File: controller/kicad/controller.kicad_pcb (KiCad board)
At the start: 2 copper layers, 132.3 x 80.9 mm, 6 parts, among them J1 pcie_98, J2 pcie_98, J3 pcie_98, J4 pcie_98, J5 pcie_98

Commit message: Auto update of the files of controller/kicad to complete the rename from main_board.
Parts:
- J1, J2, J3, J4, J5: footprint main_board:pcie_98_socket -> controller:pcie_98_socket
- RN1: footprint main_board:weact_stm32fh750 -> controller:weact_stm32fh750
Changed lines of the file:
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@@
   (net 11 "unconnected-(RN1-R2.2-Pad11)")
   (net 12 "unconnected-(RN1-R1.2-Pad12)")
-  (footprint "main_board:pcie_98_socket" (layer "F.Cu")
+  (footprint "controller:pcie_98_socket" (layer "F.Cu")
     (at 93.9 37.000004 -90)
     (tags "9-1734774-5 ")
-    (property "Sheetfile" "main_board.kicad_sch")
+    (property "Sheetfile" "controller.kicad_sch")
     (property "Sheetname" "")
     (property "ki_description" "Generic connector, double row, 02x32, row letter first pin numbering scheme (pin number consists of a letter for the row and a number for the pin index in this row. a1, ..., aN; b1, ..., bN), script generated (kicad-library-utils/schlib/autogen/connector/)")
@@
     )
   )
-  (footprint "main_board:pcie_98_socket" (layer "F.Cu")
+  (footprint "controller:pcie_98_socket" (layer "F.Cu")
     (at 109.4 36.800004 -90)
     (tags "9-1734774-5 ")
-    (property "Sheetfile" "main_board.kicad_sch")
+    (property "Sheetfile" "controller.kicad_sch")
     (property "Sheetname" "")
     (property "ki_description" "Generic connector, double row, 02x32, row letter first pin numbering scheme (pin number consists of a letter for the row and a number for the pin index in this row. a1, ..., aN; b1, ..., bN), script generated (kicad-library-utils/schlib/autogen/connector/)")
@@
     )
   )
-  (footprint "main_board:pcie_98_socket" (layer "F.Cu")
+  (footprint "controller:pcie_98_socket" (layer "F.Cu")
     (at 138.35 36.900004 -90)
     (tags "9-1734774-5 ")
-    (property "Sheetfile" "main_board.kicad_sch")
+    (property "Sheetfile" "controller.kicad_sch")
     (property "Sheetname" "")
     (property "ki_description" "Generic connector, double row, 02x32, row letter first pin numbering scheme (pin number consists of a letter for the row and a number for the pin index in this row. a1, ..., aN; b1, ..., bN), script generated (kicad-library-utils/schlib/autogen/connector/)")
@@
     )
   )
-  (footprint "main_board:pcie_98_socket" (layer "F.Cu")
+  (footprint "controller:pcie_98_socket" (layer "F.Cu")
     (at 79.4 37.100004 -90)
     (tags "9-1734774-5 ")
-    (property "Sheetfile" "main_board.kicad_sch")
+    (property "Sheetfile" "controller.kicad_sch")
     (property "Sheetname" "")
     (property "ki_description" "Generic connector, double row, 02x32, row letter first pin numbering scheme (pin number consists of a letter for the row and a number for the pin index in this row. a1, ..., aN; b1, ..., bN), script generated (kicad-library-utils/schlib/autogen/connector/)")
@@
     )
   )
-  (footprint "main_board:weact_stm32fh750" (layer "F.Cu")
+  (footprint "controller:weact_stm32fh750" (layer "F.Cu")
     (at 39.6 62.05)
     (descr "Through hole straight pin header, 2x22, 2.54mm pitch, double rows")
     (tags "Through hole pin header THT 2x22 2.54mm double row")
-    (property "Sheetfile" "main_board.kicad_sch")
+    (property "Sheetfile" "controller.kicad_sch")
     (property "Sheetname" "")
     (property "ki_description" "6 resistor network, parallel topology")
@@
     )
   )
-  (footprint "main_board:pcie_98_socket" (layer "F.Cu")
+  (footprint "controller:pcie_98_socket" (layer "F.Cu")
     (at 123.9 36.85 -90)
     (tags "9-1734774-5 ")
-    (property "Sheetfile" "main_board.kicad_sch")
+    (property "Sheetfile" "controller.kicad_sch")
     (property "Sheetname" "")
     (property "ki_description" "Generic connector, double row, 02x32, row letter first pin numbering scheme (pin number consists of a letter for the row and a number for the pin index in this row. a1, ..., aN; b1, ..., bN), script generated (kicad-library-utils/schlib/autogen/connector/)")

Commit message: Work in progress. Controller schematic.
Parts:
- removed J1, J3, J4, J5: pcie_98, controller:pcie_98_socket
- removed RN1: R_Pack06, controller:weact_stm32fh750
- added D1: ESD, Diode_SMD:D_0402_1005Metric, F.Cu at (62.2, 42.9)
- added D2: ESD, Diode_SMD:D_0402_1005Metric, F.Cu at (62.2, 40.3)
- added D3: ESD, Diode_SMD:D_0402_1005Metric, F.Cu at (63.8, 43.0)
- added D4: ESD, Diode_SMD:D_0402_1005Metric, F.Cu at (63.8, 40.4)
- added D5: ESD, Diode_SMD:D_0402_1005Metric, F.Cu at (51.2, 43.3)
- added D6: ESD, Diode_SMD:D_0402_1005Metric, F.Cu at (51.2, 45.3)
- added D7: ESD, Diode_SMD:D_0402_1005Metric, F.Cu at (51.2, 47.3)
- added D8: ESD, Diode_SMD:D_0402_1005Metric, F.Cu at (51.2, 49.2)
- added D9: ESD, Diode_SMD:D_0402_1005Metric, F.Cu at (51.2, 51.2)
- added U1: WeAct_STM32H750_Module, controller:weact_stm32fh750, F.Cu at (85.2, -5.38)
- J2: footprint controller:pcie_98_socket -> controller:pcie_98_edge
- moved J2 26.3 mm to (72.5, 62.5), turned to 0 degrees
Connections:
- J2 pad A1: (no net) -> GND
- J2 pad A10: (no net) -> /A
- J2 pad A11: (no net) -> /A
- J2 pad A12: (no net) -> /A
- J2 pad A13: (no net) -> /A
- J2 pad A14: (no net) -> /A
- J2 pad A15: (no net) -> /A
- J2 pad A16: (no net) -> /A
- J2 pad A17: (no net) -> /A
- J2 pad A18: (no net) -> /A
- J2 pad A19: (no net) -> /A
- J2 pad A2: (no net) -> GND
- J2 pad A20: (no net) -> /A
- J2 pad A21: (no net) -> /A
- J2 pad A22: (no net) -> /A
- J2 pad A23: (no net) -> /A
- J2 pad A24: (no net) -> /A
- J2 pad A25: (no net) -> /A
- J2 pad A26: (no net) -> /A
- J2 pad A27: (no net) -> /A
- J2 pad A28: (no net) -> /A
- J2 pad A29: (no net) -> /A
- J2 pad A3: (no net) -> GND
- J2 pad A30: (no net) -> /A
- J2 pad A31: (no net) -> /A
- J2 pad A32: (no net) -> /A
- J2 pad A33: (no net) -> /A
- J2 pad A34: (no net) -> /A
- J2 pad A35: (no net) -> /A
- J2 pad A36: (no net) -> /A
- J2 pad A37: (no net) -> /A
- J2 pad A38: (no net) -> /A
- J2 pad A39: (no net) -> /A
- J2 pad A4: (no net) -> GND
- J2 pad A40: (no net) -> /A
- J2 pad A41: (no net) -> /A
- J2 pad A42: (no net) -> /A
- J2 pad A43: (no net) -> /A
- J2 pad A44: (no net) -> /A
- J2 pad A45: (no net) -> /A
- J2 pad A46: (no net) -> /A
- J2 pad A47: (no net) -> /A
- J2 pad A48: (no net) -> /VIN-
- J2 pad A49: (no net) -> /VIN-
- J2 pad A5: (no net) -> /PE0
- J2 pad A6: (no net) -> /PB8
- J2 pad A7: (no net) -> /PB6
- J2 pad A8: (no net) -> /PB4
- J2 pad A9: (no net) -> /PD7
- J2 pad B1: (no net) -> +5V
- J2 pad B10: (no net) -> /B
- J2 pad B11: (no net) -> /B
- J2 pad B12: (no net) -> /B
- J2 pad B13: (no net) -> /B
- J2 pad B14: (no net) -> /B
- J2 pad B15: (no net) -> /B
- J2 pad B16: (no net) -> /B
- J2 pad B17: (no net) -> /B
- J2 pad B18: (no net) -> /B
- J2 pad B19: (no net) -> /B
- J2 pad B2: (no net) -> +5V
- J2 pad B20: (no net) -> /B
- J2 pad B21: (no net) -> /B
- J2 pad B22: (no net) -> /B
- J2 pad B23: (no net) -> /B
- J2 pad B3: (no net) -> +5V
- J2 pad B4: (no net) -> +5V
- J2 pad B5: (no net) -> /PE1
- J2 pad B6: (no net) -> /PB9
- J2 pad B7: (no net) -> /PB7
- J2 pad B8: (no net) -> /PB5
- J2 pad B9: (no net) -> /PB3
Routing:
- net /PE1: track 0.00 -> 97.2 mm
- net /PB9: track 0.00 -> 95.1 mm
- net /PB5: track 0.00 -> 20.9 mm
- net /PB7: track 0.00 -> 17.8 mm
- net GND: track 0.00 -> 1.77 mm, vias 0 -> 4
- net (no net): vias 0 -> 1
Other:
- board size 132.3 x 80.9 mm -> 58.6 x 9.3 mm

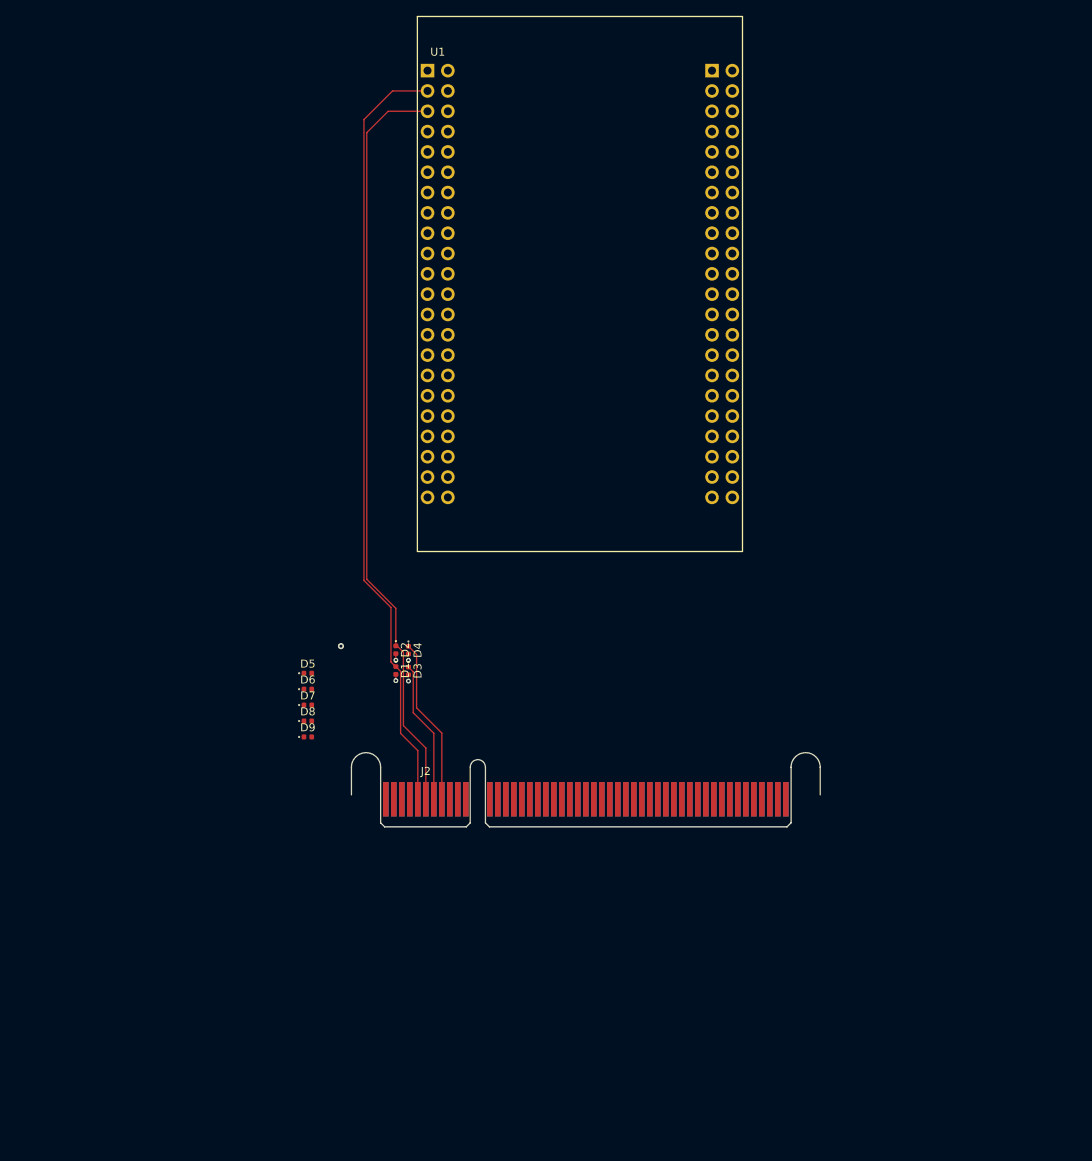
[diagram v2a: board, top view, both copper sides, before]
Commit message: Controller design in progress. Added ESD diode arrays.
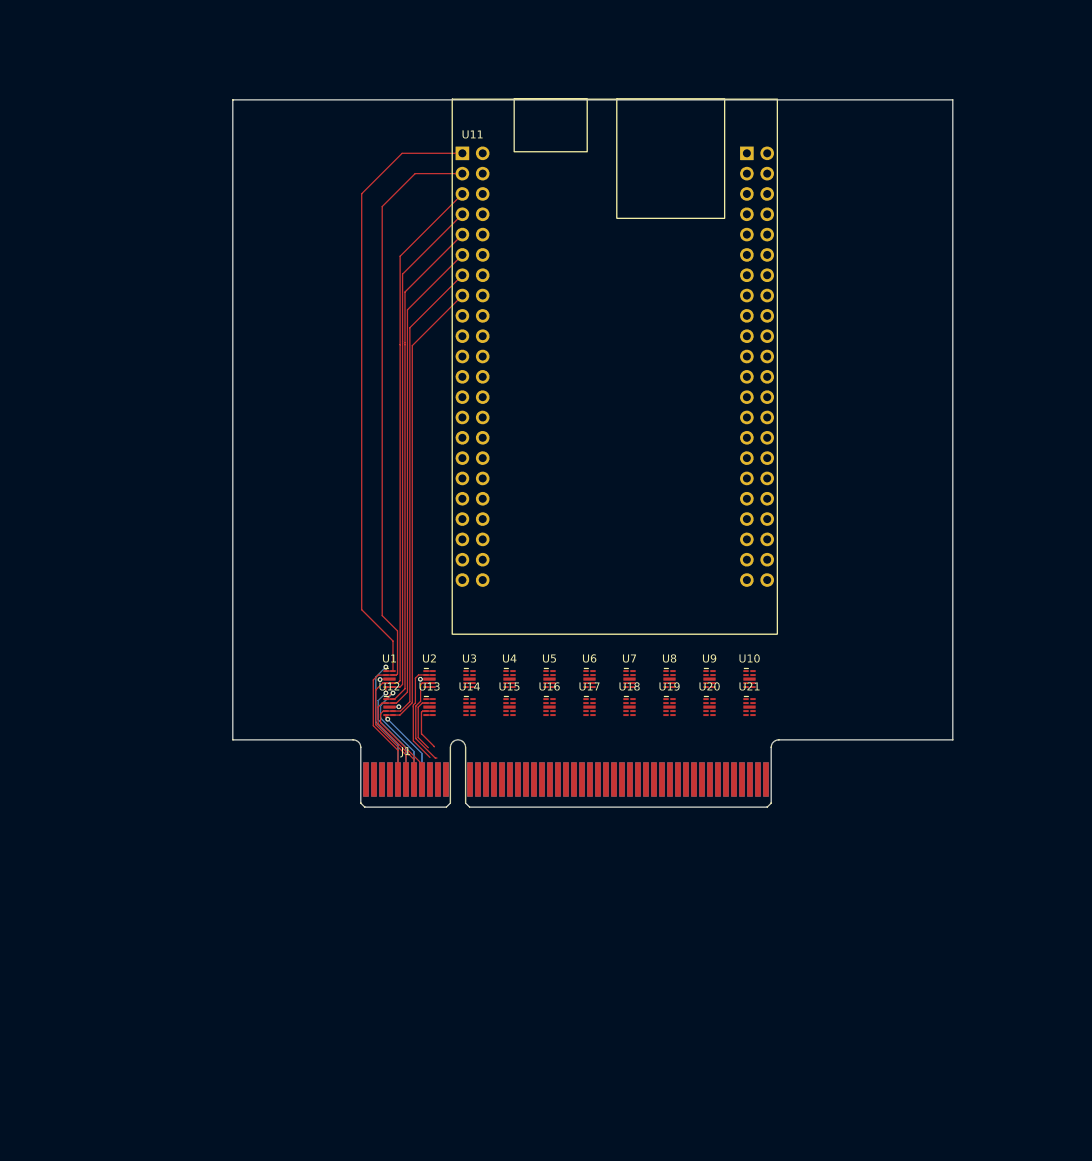
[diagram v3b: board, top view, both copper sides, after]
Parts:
- removed D1, D2, D3, D4, D5, D6, D7, D8, D9: ESD, Diode_SMD:D_0402_1005Metric
- added U1: ESD5344D, controller:Diodes_UDFN-10_1.0x2.5mm_P0.5mm, F.Cu at (61.4, 44.0)
- added U10: ESD5344D, controller:Diodes_UDFN-10_1.0x2.5mm_P0.5mm, F.Cu at (106.4, 44.0)
- added U12: ESD5344D, controller:Diodes_UDFN-10_1.0x2.5mm_P0.5mm, F.Cu at (61.4, 47.5)
- added U13: ESD5344D, controller:Diodes_UDFN-10_1.0x2.5mm_P0.5mm, F.Cu at (66.4, 47.5)
- added U14: ESD5344D, controller:Diodes_UDFN-10_1.0x2.5mm_P0.5mm, F.Cu at (71.4, 47.5)
- added U15: ESD5344D, controller:Diodes_UDFN-10_1.0x2.5mm_P0.5mm, F.Cu at (76.4, 47.5)
- added U16: ESD5344D, controller:Diodes_UDFN-10_1.0x2.5mm_P0.5mm, F.Cu at (81.4, 47.5)
- added U17: ESD5344D, controller:Diodes_UDFN-10_1.0x2.5mm_P0.5mm, F.Cu at (86.4, 47.5)
- added U18: ESD5344D, controller:Diodes_UDFN-10_1.0x2.5mm_P0.5mm, F.Cu at (91.4, 47.5)
- added U19: ESD5344D, controller:Diodes_UDFN-10_1.0x2.5mm_P0.5mm, F.Cu at (96.4, 47.5)
- added U2: ESD5344D, controller:Diodes_UDFN-10_1.0x2.5mm_P0.5mm, F.Cu at (66.4, 44.0)
- added U20: ESD5344D, controller:Diodes_UDFN-10_1.0x2.5mm_P0.5mm, F.Cu at (101.4, 47.5)
- added U21: ESD5344D, controller:Diodes_UDFN-10_1.0x2.5mm_P0.5mm, F.Cu at (106.4, 47.5)
- added U3: ESD5344D, controller:Diodes_UDFN-10_1.0x2.5mm_P0.5mm, F.Cu at (71.4, 44.0)
- added U4: ESD5344D, controller:Diodes_UDFN-10_1.0x2.5mm_P0.5mm, F.Cu at (76.4, 44.0)
- added U5: ESD5344D, controller:Diodes_UDFN-10_1.0x2.5mm_P0.5mm, F.Cu at (81.4, 44.0)
- added U6: ESD5344D, controller:Diodes_UDFN-10_1.0x2.5mm_P0.5mm, F.Cu at (86.4, 44.0)
- added U7: ESD5344D, controller:Diodes_UDFN-10_1.0x2.5mm_P0.5mm, F.Cu at (91.4, 44.0)
- added U8: ESD5344D, controller:Diodes_UDFN-10_1.0x2.5mm_P0.5mm, F.Cu at (96.4, 44.0)
- added U9: ESD5344D, controller:Diodes_UDFN-10_1.0x2.5mm_P0.5mm, F.Cu at (101.4, 44.0)
- moved U11 11.2 mm to (89.6, 4.95)
- moved J1 3.50 mm to (70.0, 60.0)
- renumbered J2 to J1, U1 to U11
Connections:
- J1 pad A10: /A -> /PB1
- J1 pad A11: /A -> /PE7
- J1 pad A12: /A -> /PE13
- J1 pad A13: /A -> /PB15
- J1 pad A5: /PE0 -> /PB13
- J1 pad A6: /PB8 -> /PD11
- J1 pad A7: /PB6 -> /PD13
- J1 pad A8: /PB4 -> /PC9
- J1 pad A9: /PD7 -> /PC5
- J1 pad B10: /B -> /PE9
- J1 pad B11: /B -> /PE11
- J1 pad B12: /B -> /PB11
- J1 pad B5: /PE1 -> /PB15
- J1 pad B6: /PB9 -> /PD9
- J1 pad B7: /PB7 -> /PD15
- J1 pad B8: /PB5 -> /PC7
- U11 pad 1: GND -> /PB13
- U11 pad 10: /PB4 -> /PD12
- U11 pad 11: /PB3 -> /PD15
- U11 pad 12: /PD7 -> /PD14
- U11 pad 13: /PD6 -> /PC7
- U11 pad 14: /PD5 -> /PC6
- U11 pad 15: /PD4 -> /PC9
- U11 pad 16: /PD3 -> /PC8
- U11 pad 17: /PD2 -> /PA9
- U11 pad 18: /PD1 -> /PA8
- U11 pad 19: /PD0 -> /PA11
- U11 pad 2: +5V -> /PB12
- U11 pad 20: /PC12 -> /PA10
- U11 pad 21: /PC11 -> /PA15
- U11 pad 22: /PC10 -> /PA12
- U11 pad 23: /PA15 -> /PC11
- U11 pad 24: /PA12 -> /PC10
- U11 pad 25: /PA11 -> /PD0
- U11 pad 26: /PA10 -> /PC12
- U11 pad 27: /PA9 -> /PD2
- U11 pad 28: /PA8 -> /PD1
- U11 pad 29: /PC9 -> /PD4
- U11 pad 3: /PE1 -> /PB15
- U11 pad 30: /PC8 -> /PD3
- U11 pad 31: /PC7 -> /PD6
- U11 pad 32: /PC6 -> /PD5
- U11 pad 33: /PD15 -> /PB3
- U11 pad 34: /PD14 -> /PD7
- U11 pad 35: /PD13 -> /PB5
- U11 pad 36: /PD12 -> /PB4
- U11 pad 37: /PD11 -> /PB7
- U11 pad 38: /PD10 -> /PB6
- U11 pad 39: /PD9 -> /PB9
- U11 pad 4: /PE0 -> /PB14
- U11 pad 40: /PD8 -> /PB8
- U11 pad 41: /PB15 -> /PE1
- U11 pad 42: /PB14 -> /PE0
- U11 pad 43: /PB13 -> GND
- U11 pad 44: /PB12 -> +5V
- U11 pad 46: +3V3 -> GND
- U11 pad 47: /PE2 -> +3V3
- U11 pad 48: /XX -> +5V
- U11 pad 49: /PE4 -> /PB10
- U11 pad 5: /PB9 -> /PD9
- U11 pad 50: /XX -> /PB11
- U11 pad 51: /PE6 -> /PE14
- U11 pad 52: /XX -> /PE15
- U11 pad 53: /PC13 -> /PE12
- U11 pad 54: /XX -> /PE13
- U11 pad 6: /PB8 -> /PD8
- U11 pad 7: /PB7 -> /PD11
- U11 pad 8: /PB6 -> /PD10
- U11 pad 9: /PB5 -> /PD13
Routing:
- net /PE1: track 97.2 -> 0.00 mm
- net /PB9: track 95.1 -> 0.00 mm
- net /PB13: track 0.00 -> 93.1 mm, vias 0 -> 1
- net /PB15: track 0.00 -> 88.0 mm
- net /PD9: track 0.00 -> 80.3 mm
- net /PD11: track 0.00 -> 77.5 mm, vias 0 -> 1
- net /PD13: track 0.00 -> 77.0 mm, vias 0 -> 1
- net /PD15: track 0.00 -> 72.8 mm
- net /PC7: track 0.00 -> 70.7 mm
- net /PC9: track 0.00 -> 67.3 mm, vias 0 -> 1
- net /PB5: track 20.9 -> 0.00 mm
- net /PB7: track 17.8 -> 0.00 mm
- net /PA11: track 0.00 -> 13.3 mm
- net /PA15: track 0.00 -> 12.3 mm
- net /PD2: track 0.00 -> 7.66 mm
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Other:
- board size 58.6 x 9.3 mm -> 90 x 80 mm

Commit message: Work in progress. Rouging the MCU signals.
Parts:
- moved U1 1.15 mm to (62.0, 45.0)
- moved U10 1.15 mm to (107.0, 45.0)
- moved U11 1.15 mm to (90.2, 5.95)
- moved U12 1.15 mm to (62.0, 48.5)
- moved U13 1.15 mm to (67.0, 48.5)
- moved U14 1.15 mm to (72.0, 48.5)
- moved U15 1.15 mm to (77.0, 48.5)
- moved U16 1.15 mm to (82.0, 48.5)
- moved U17 1.15 mm to (87.0, 48.5)
- moved U18 1.15 mm to (92.0, 48.5)
- moved U19 1.15 mm to (97.0, 48.5)
- moved U2 1.15 mm to (67.0, 45.0)
- moved U20 1.15 mm to (102.0, 48.5)
- moved U21 1.15 mm to (107.0, 48.5)
- moved U3 1.15 mm to (72.0, 45.0)
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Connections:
- J1 pad A10: /PB1 -> /PC11
- J1 pad A11: /PE7 -> /PD0
- J1 pad A12: /PE13 -> /PD6
- J1 pad A13: /PB15 -> /PB3
- J1 pad A14: /A -> /PB9
- J1 pad A15: /A -> /PE1
- J1 pad A16: /A -> /PB6
- J1 pad A9: /PC5 -> /PA9
- J1 pad B10: /PE9 -> /PA15
- J1 pad B11: /PE11 -> /PD2
- J1 pad B12: /PB11 -> /PD4
- J1 pad B13: /B -> /PB5
- J1 pad B14: /B -> /PB7
- J1 pad B15: /B -> /PE0
- J1 pad B16: /B -> /PB8
- J1 pad B9: /PB3 -> /PA11
- U10 pad 1: unconnected-(U10-Pad1) -> /X
- U10 pad 2: unconnected-(U10-Pad2) -> /X
- U10 pad 4: unconnected-(U10-Pad4) -> /X
- U10 pad 5: unconnected-(U10-Pad5) -> /X
- U14 pad 1: unconnected-(U14-Pad1) -> /PE1
- U14 pad 2: unconnected-(U14-Pad2) -> /PE0
- U14 pad 4: unconnected-(U14-Pad4) -> /PB8
- U14 pad 5: unconnected-(U14-Pad5) -> /PB6
- U15 pad 1: unconnected-(U15-Pad1) -> /X
- U15 pad 2: unconnected-(U15-Pad2) -> /X
- U15 pad 4: unconnected-(U15-Pad4) -> /X
- U15 pad 5: unconnected-(U15-Pad5) -> /X
- U16 pad 1: unconnected-(U16-Pad1) -> /X
- U16 pad 2: unconnected-(U16-Pad2) -> /X
- U16 pad 4: unconnected-(U16-Pad4) -> /X
- U16 pad 5: unconnected-(U16-Pad5) -> /X
- U17 pad 1: unconnected-(U17-Pad1) -> /X
- U17 pad 2: unconnected-(U17-Pad2) -> /X
- U17 pad 4: unconnected-(U17-Pad4) -> /X
- U17 pad 5: unconnected-(U17-Pad5) -> /X
- U18 pad 1: unconnected-(U18-Pad1) -> /X
- U18 pad 2: unconnected-(U18-Pad2) -> /X
- U18 pad 4: unconnected-(U18-Pad4) -> /X
- U18 pad 5: unconnected-(U18-Pad5) -> /X
- U19 pad 1: unconnected-(U19-Pad1) -> /X
- U19 pad 2: unconnected-(U19-Pad2) -> /X
- U19 pad 4: unconnected-(U19-Pad4) -> /X
- U19 pad 5: unconnected-(U19-Pad5) -> /X
- U20 pad 1: unconnected-(U20-Pad1) -> /X
- U20 pad 2: unconnected-(U20-Pad2) -> /X
- U20 pad 4: unconnected-(U20-Pad4) -> /X
- U20 pad 5: unconnected-(U20-Pad5) -> /X
- U21 pad 1: unconnected-(U21-Pad1) -> /X
- U21 pad 2: unconnected-(U21-Pad2) -> /X
- U21 pad 4: unconnected-(U21-Pad4) -> /X
- U21 pad 5: unconnected-(U21-Pad5) -> /X
- U3 pad 1: unconnected-(U3-Pad1) -> /PB3
- U3 pad 2: unconnected-(U3-Pad2) -> /PB5
- U3 pad 4: unconnected-(U3-Pad4) -> /PB7
- U3 pad 5: unconnected-(U3-Pad5) -> /PB9
- U4 pad 1: unconnected-(U4-Pad1) -> /X
- U4 pad 2: unconnected-(U4-Pad2) -> /X
- U4 pad 4: unconnected-(U4-Pad4) -> /X
- U4 pad 5: unconnected-(U4-Pad5) -> /X
- U5 pad 1: unconnected-(U5-Pad1) -> /X
- U5 pad 2: unconnected-(U5-Pad2) -> /X
- U5 pad 4: unconnected-(U5-Pad4) -> /X
- U5 pad 5: unconnected-(U5-Pad5) -> /X
- U6 pad 1: unconnected-(U6-Pad1) -> /X
- U6 pad 2: unconnected-(U6-Pad2) -> /X
- U6 pad 4: unconnected-(U6-Pad4) -> /X
- U6 pad 5: unconnected-(U6-Pad5) -> /X
- U7 pad 1: unconnected-(U7-Pad1) -> /X
- U7 pad 2: unconnected-(U7-Pad2) -> /X
- U7 pad 4: unconnected-(U7-Pad4) -> /X
- U7 pad 5: unconnected-(U7-Pad5) -> /X
- U8 pad 1: unconnected-(U8-Pad1) -> /X
- U8 pad 2: unconnected-(U8-Pad2) -> /X
- U8 pad 4: unconnected-(U8-Pad4) -> /X
- U8 pad 5: unconnected-(U8-Pad5) -> /X
- U9 pad 1: unconnected-(U9-Pad1) -> /X
- U9 pad 2: unconnected-(U9-Pad2) -> /X
- U9 pad 4: unconnected-(U9-Pad4) -> /X
- U9 pad 5: unconnected-(U9-Pad5) -> /X
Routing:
- net /PA9: track 0.88 -> 63.0 mm, vias 0 -> 1
- net /PC11: track 0.88 -> 55.0 mm, vias 0 -> 1
- net /PD0: track 0.88 -> 54.1 mm, vias 0 -> 1
- net /PA11: track 13.3 -> 60.8 mm
- net /PD6: track 0.88 -> 47.4 mm, vias 0 -> 1
- net /PA15: track 12.3 -> 58.1 mm
- net /PD4: track 6.49 -> 51.5 mm
- net /PB3: track 0.00 -> 43.2 mm, vias 0 -> 1
- net /PD2: track 7.66 -> 50.5 mm
- net /PB5: track 0.00 -> 40.8 mm
- net /PB7: track 0.00 -> 38.2 mm
- net /PB6: track 0.00 -> 36.4 mm, vias 0 -> 1
- net /PB9: track 0.00 -> 35.1 mm, vias 0 -> 1
- net /PB8: track 0.00 -> 34.4 mm
- net /PE1: track 0.00 -> 33.5 mm, vias 0 -> 1
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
